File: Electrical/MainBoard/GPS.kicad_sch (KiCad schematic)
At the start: 2 parts, among them U7 MAX-M8C-0

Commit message: Begin layout of pcb
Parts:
- added E1: APAE1590R2540AKDB1-T, RobotLibrary:XDCR_APAE1590R2540AKDB1-T, symbol RobotLibary:APAE1590R2540AKDB1-T
- renumbered U7 to U14
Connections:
- net at U14.11 (RF_IN): now also E1.1
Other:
- note removed: "Antenna DigiKey PN: 2057-ANT-20087EB56-ND Maybe?..."
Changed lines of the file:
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@@
+    (stroke (width 0) (type default))
+  )
+  (wire (pts (xy 79.375 93.345) (xy 105.41 93.345))
     (stroke (width 0) (type default))
   )
@@
     (stroke (width 0) (type default))
   )
+  (wire (pts (xy 79.375 91.44) (xy 79.375 93.345))
+    (stroke (width 0) (type default))
+  )
   (wire (pts (xy 158.75 186.055) (xy 161.925 186.055))
     (stroke (width 0) (type default))
@@
   (wire (pts (xy 99.06 90.805) (xy 105.41 90.805))
     (stroke (width 0) (type default))
-  )
-  (text "Antenna DigiKey PN: 2057-ANT-20087EB56-ND\nMaybe?..."
-    (at 38.1 95.885 0)
-    (effects (font (size 1.27 1.27)) (justify left bottom))
   )
   (hierarchical_label "U2RX" (shape output) (at 155.575 103.505 0) (fields_autoplaced)
@@
         )
         (path "/bd24c4db-4e36-4117-bd4f-5228ef241da9/3efd4746-229a-4377-9033-64e7155c364f"
-          (reference "#PWR083") (unit 1)
+          (reference "#PWR0150") (unit 1)
         )
       )
@@
   (symbol (lib_id "RobotLibary:MAX-M8C-0") (at 128.27 95.885 0) (unit 1)
     (in_bom yes) (on_board yes) (dnp no)
-    (property "Reference" "U7" (at 128.27 74.295 0)
+    (property "Reference" "U14" (at 128.27 74.295 0)
       (effects (font (size 2 2)))
     )
@@
       (project "MainBoard"
         (path "/bd24c4db-4e36-4117-bd4f-5228ef241da9/3efd4746-229a-4377-9033-64e7155c364f"
-          (reference "U7") (unit 1)
+          (reference "U14") (unit 1)
         )
       )
@@
         )
         (path "/bd24c4db-4e36-4117-bd4f-5228ef241da9/3efd4746-229a-4377-9033-64e7155c364f"
-          (reference "C17") (unit 1)
+          (reference "C34") (unit 1)
         )
       )
@@
         )
         (path "/bd24c4db-4e36-4117-bd4f-5228ef241da9/3efd4746-229a-4377-9033-64e7155c364f"
-          (reference "#PWR082") (unit 1)
+          (reference "#PWR0146") (unit 1)
+        )
+      )
+    )
+  )
+  (symbol (lib_id "RobotLibary:APAE1590R2540AKDB1-T") (at 79.375 86.36 0) (unit 1)
+    (in_bom yes) (on_board yes) (dnp no) (fields_autoplaced)
+    (property "Reference" "E1" (at 83.185 83.6295 0)
+      (effects (font (size 1.27 1.27)) (justify left))
+    )
+    (property "Value" "APAE1590R2540AKDB1-T" (at 83.185 86.1695 0)
+      (effects (font (size 1.27 1.27)) (justify left))
+    )
+    (property "Footprint" "RobotLibrary:XDCR_APAE1590R2540AKDB1-T" (at 79.375 86.36 0)
+      (effects (font (size 1.27 1.27)) (justify bottom) hide)
+    )
+    (property "Datasheet" "https://abracon.com/patchantenna/APAE1590R2540AKDB1-T.pdf" (at 79.375 86.36 0)
+      (effects (font (size 1.27 1.27)) hide)
+    )
+    (property "Description" "RF ANT 1.575/1.602GHZ CER PATCH" (at 79.375 86.36 0)
+      (effects (font (size 1.27 1.27)) hide)
+    )
+    (property "Mfr" "Abracon LLC" (at 79.375 86.36 0)
+      (effects (font (size 1.27 1.27)) hide)
+    )
+    (property "Mfr P/N" "APAE1590R2540AKDB1-T" (at 79.375 86.36 0)
+      (effects (font (size 1.27 1.27)) hide)
+    )
+    (property "Supplier 1" "DigiKey" (at 79.375 86.36 0)
+      (effects (font (size 1.27 1.27)) hide)
+    )
+    (property "Supplier 1 P/N" "535-11940-ND" (at 79.375 86.36 0)
+      (effects (font (size 1.27 1.27)) hide)
+    )
+    (property "Supplier 2" "" (at 79.375 86.36 0)
+      (effects (font (size 1.27 1.27)) hide)
+    )
+    (property "Supplier 2 P/N" "" (at 79.375 86.36 0)
+      (effects (font (size 1.27 1.27)) hide)
+    )
+    (pin "1")
+    (instances
+      (project "MainBoard"
+        (path "/bd24c4db-4e36-4117-bd4f-5228ef241da9/3efd4746-229a-4377-9033-64e7155c364f"
+          (reference "E1") (unit 1)
         )
       )
@@
         )
         (path "/bd24c4db-4e36-4117-bd4f-5228ef241da9/3efd4746-229a-4377-9033-64e7155c364f"
-          (reference "#PWR080") (unit 1)
+          (reference "#PWR0148") (unit 1)
         )
       )
@@
         )
         (path "/bd24c4db-4e36-4117-bd4f-5228ef241da9/3efd4746-229a-4377-9033-64e7155c364f"
-          (reference "#PWR079") (unit 1)
+          (reference "#PWR0147") (unit 1)
         )
       )
@@
         )
         (path "/bd24c4db-4e36-4117-bd4f-5228ef241da9/3efd4746-229a-4377-9033-64e7155c364f"
-          (reference "#PWR081") (unit 1)
-        )
-      )
+          (reference "#PWR0149") (unit 1)
+        )
+      )

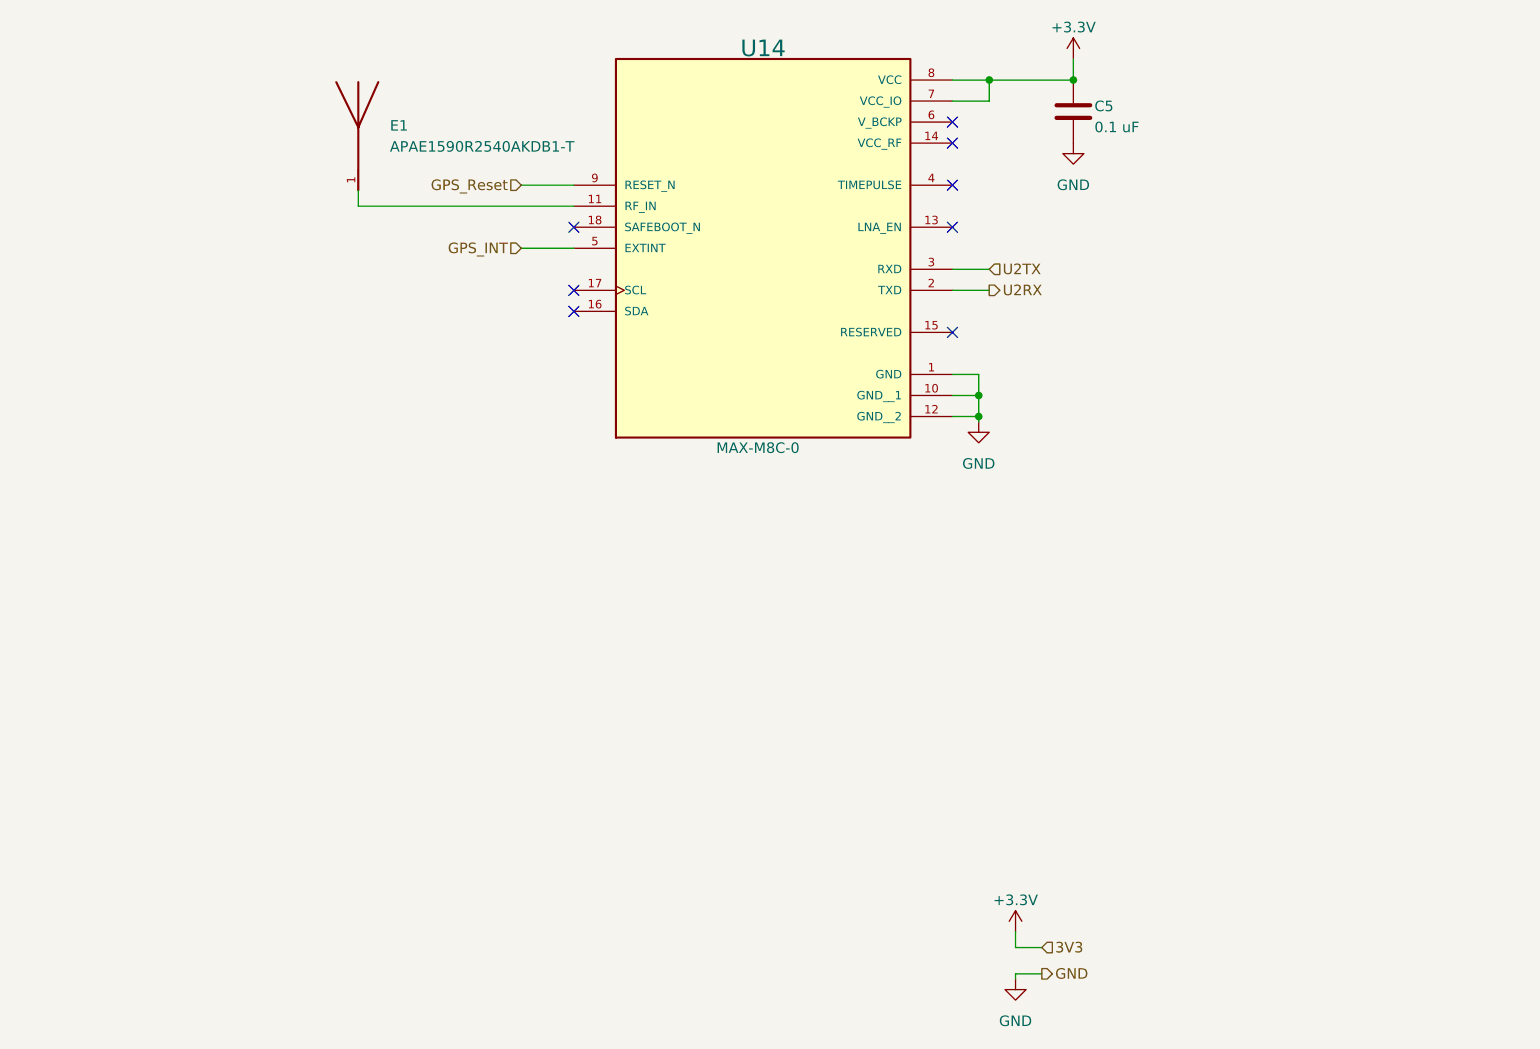
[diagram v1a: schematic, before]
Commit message: First Pass at the routing
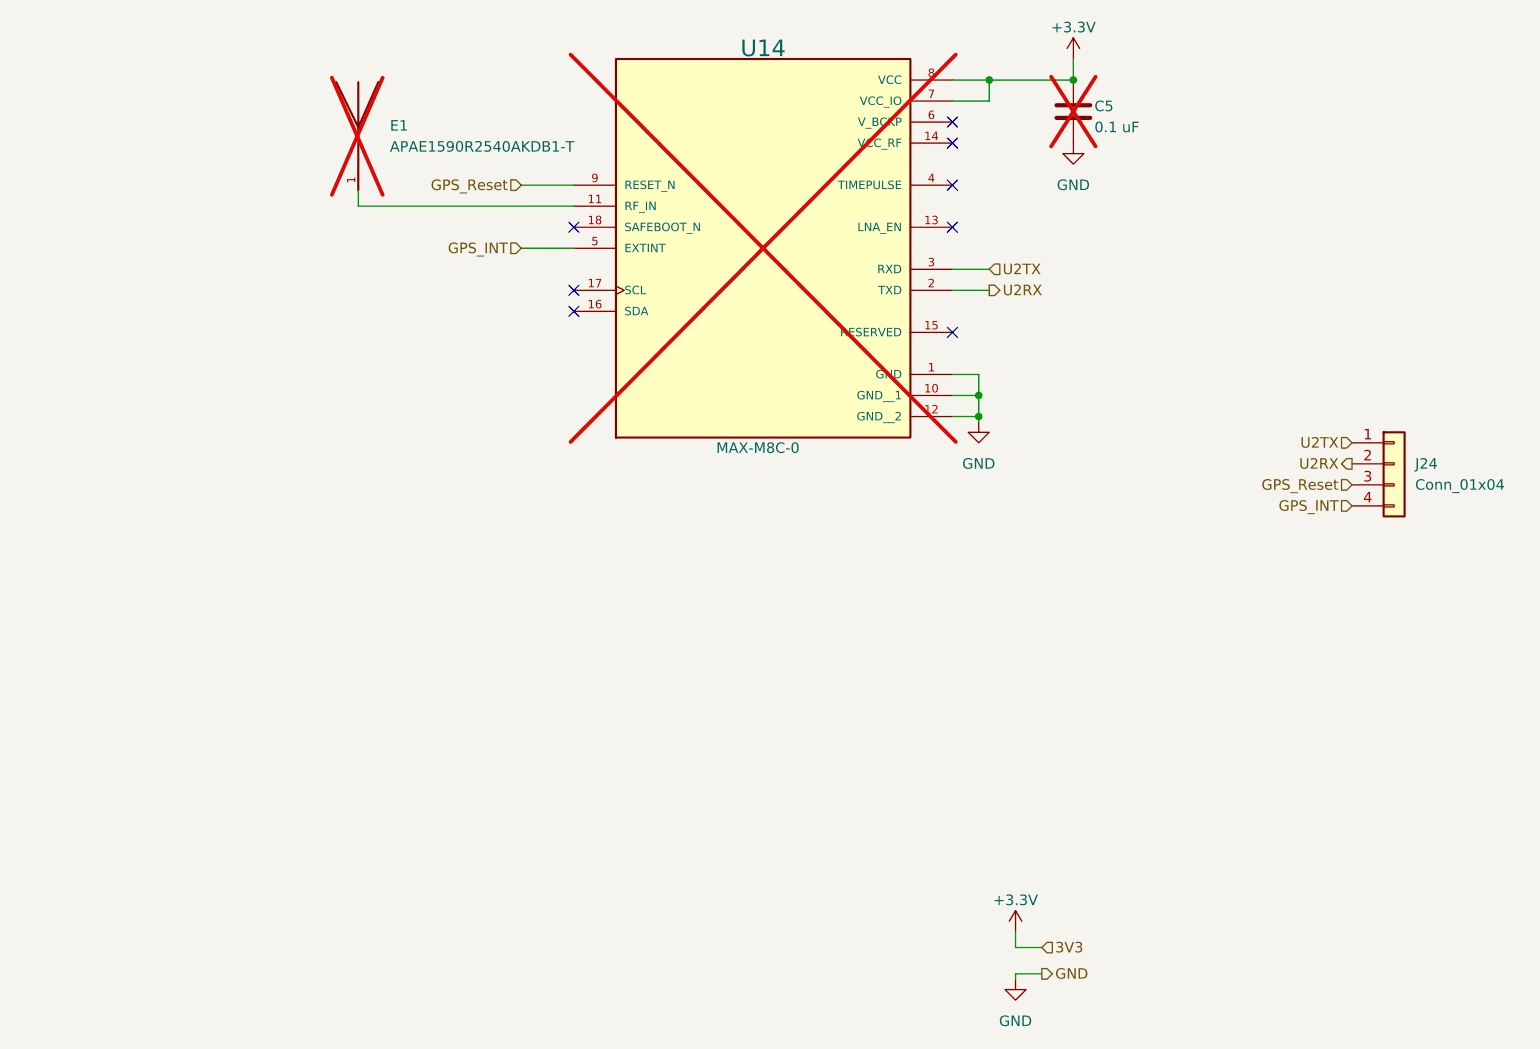
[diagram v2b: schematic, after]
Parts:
- added J24: Conn_01x04, RobotLibrary:CONN_22-23-2041_MOL, symbol Connector_Generic:Conn_01x04
- C5, U14: now not fitted; now left out of the parts list
- E1: MANUFACTURER (none) -> Abracon; MAXIMUM_PACKAGE_HEIGHT (none) -> 4.7mm; PARTREV (none) -> -; SNAPEDA_PN (none) -> APAE1590R2540AKDB1-T; STANDARD (none) -> IPC-7351B; now not fitted; now left out of the parts list
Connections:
- net GPS_INT: now also J24.4 (Pin_4)
- net GPS_Reset: now also J24.3 (Pin_3)
- net U2RX: now also J24.2 (Pin_2)
- net U2TX: now also J24.1 (Pin_1)
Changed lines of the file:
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@@
     (stroke (width 0) (type default))
   )
+  (hierarchical_label "GPS_Reset" (shape input) (at 199.39 127 180) (fields_autoplaced)
+    (effects (font (size 1.27 1.27)) (justify right))
+  )
   (hierarchical_label "U2RX" (shape output) (at 155.575 103.505 0) (fields_autoplaced)
     (effects (font (size 1.27 1.27)) (justify left))
@@
     (effects (font (size 1.27 1.27)) (justify left))
   )
+  (hierarchical_label "U2RX" (shape output) (at 199.39 124.46 180) (fields_autoplaced)
+    (effects (font (size 1.27 1.27)) (justify right))
+  )
   (hierarchical_label "GPS_INT" (shape input) (at 99.06 98.425 180) (fields_autoplaced)
     (effects (font (size 1.27 1.27)) (justify right))
   )
+  (hierarchical_label "U2TX" (shape input) (at 199.39 121.92 180) (fields_autoplaced)
+    (effects (font (size 1.27 1.27)) (justify right))
+  )
+  (hierarchical_label "U2TX" (shape input) (at 155.575 100.965 0) (fields_autoplaced)
+    (effects (font (size 1.27 1.27)) (justify left))
+  )
   (hierarchical_label "GPS_Reset" (shape input) (at 99.06 90.805 180) (fields_autoplaced)
     (effects (font (size 1.27 1.27)) (justify right))
   )
-  (hierarchical_label "U2TX" (shape input) (at 155.575 100.965 0) (fields_autoplaced)
-    (effects (font (size 1.27 1.27)) (justify left))
+  (hierarchical_label "GPS_INT" (shape input) (at 199.39 129.54 180) (fields_autoplaced)
+    (effects (font (size 1.27 1.27)) (justify right))
   )
   (symbol (lib_id "power:GND") (at 165.735 85.725 0) (unit 1)
@@
     )
   )
+  (symbol (lib_id "Connector_Generic:Conn_01x04") (at 204.47 124.46 0) (unit 1)
+    (in_bom yes) (on_board yes) (dnp no) (fields_autoplaced)
+    (property "Reference" "J24" (at 207.01 124.46 0)
+      (effects (font (size 1.27 1.27)) (justify left))
+    )
+    (property "Value" "Conn_01x04" (at 207.01 127 0)
+      (effects (font (size 1.27 1.27)) (justify left))
+    )
+    (property "Footprint" "RobotLibrary:CONN_22-23-2041_MOL" (at 204.47 124.46 0)
+      (effects (font (size 1.27 1.27)) hide)
+    )
+    (property "Datasheet" "~" (at 204.47 124.46 0)
+      (effects (font (size 1.27 1.27)) hide)
+    )
+    (property "Description" "" (at 204.47 124.46 0)
+      (effects (font (size 1.27 1.27)) hide)
+    )
+    (property "Mfr" "" (at 204.47 124.46 0)
+      (effects (font (size 1.27 1.27)) hide)
+    )
+    (property "Mfr P/N" "" (at 204.47 124.46 0)
+      (effects (font (size 1.27 1.27)) hide)
+    )
+    (property "Supplier 1" "" (at 204.47 124.46 0)
+      (effects (font (size 1.27 1.27)) hide)
+    )
+    (property "Supplier 1 P/N" "" (at 204.47 124.46 0)
+      (effects (font (size 1.27 1.27)) hide)
+    )
+    (property "Supplier 2" "" (at 204.47 124.46 0)
+      (effects (font (size 1.27 1.27)) hide)
+    )
+    (property "Supplier 2 P/N" "" (at 204.47 124.46 0)
+      (effects (font (size 1.27 1.27)) hide)
+    )
+    (pin "1")
+    (pin "2")
+    (pin "3")
+    (pin "4")
+    (instances
+      (project "MainBoard"
+        (path "/bd24c4db-4e36-4117-bd4f-5228ef241da9/3efd4746-229a-4377-9033-64e7155c364f"
+          (reference "J24") (unit 1)
+        )
+      )
+    )
+  )
   (symbol (lib_id "RobotLibary:MAX-M8C-0") (at 128.27 95.885 0) (unit 1)
-    (in_bom yes) (on_board yes) (dnp no)
+    (in_bom no) (on_board no) (dnp yes)
     (property "Reference" "U14" (at 128.27 74.295 0)
       (effects (font (size 2 2)))
@@
     )
     (property "Datasheet" "https://www.u-blox.com/en/docs/UBX-16000093" (at 128.27 95.885 0)
+      (effects (font (size 1.27 1.27)) hide)
+    )
+    (property "Description" "" (at 128.27 95.885 0)
+      (effects (font (size 1.27 1.27)) hide)
+    )
+    (property "Mfr" "" (at 128.27 95.885 0)
+      (effects (font (size 1.27 1.27)) hide)
+    )
+    (property "Mfr P/N" "" (at 128.27 95.885 0)
+      (effects (font (size 1.27 1.27)) hide)
+    )
+    (property "Supplier 1" "" (at 128.27 95.885 0)
+      (effects (font (size 1.27 1.27)) hide)
+    )
+    (property "Supplier 1 P/N" "" (at 128.27 95.885 0)
+      (effects (font (size 1.27 1.27)) hide)
+    )
+    (property "Supplier 2" "" (at 128.27 95.885 0)
+      (effects (font (size 1.27 1.27)) hide)
+    )
+    (property "Supplier 2 P/N" "" (at 128.27 95.885 0)
       (effects (font (size 1.27 1.27)) hide)
     )
@@
   )
   (symbol (lib_id "Device:C") (at 165.735 81.915 0) (unit 1)
-    (in_bom yes) (on_board yes) (dnp no)
+    (in_bom no) (on_board no) (dnp yes)
     (property "Reference" "C5" (at 168.275 81.28 0)
       (effects (font (size 1.27 1.27)) (justify left))
@@
   )
   (symbol (lib_id "RobotLibary:APAE1590R2540AKDB1-T") (at 79.375 86.36 0) (unit 1)
-    (in_bom yes) (on_board yes) (dnp no) (fields_autoplaced)
+    (in_bom no) (on_board no) (dnp yes) (fields_autoplaced)
     (property "Reference" "E1" (at 83.185 83.6295 0)
       (effects (font (size 1.27 1.27)) (justify left))
@@
       (effects (font (size 1.27 1.27)) hide)
     )
-    (pin "1")
+    (property "PARTREV" "-" (at 79.375 86.36 0)
+      (effects (font (size 1.27 1.27)) (justify bottom) hide)
+    )
+    (property "SNAPEDA_PN" "APAE1590R2540AKDB1-T" (at 79.375 86.36 0)
+      (effects (font (size 1.27 1.27)) (justify bottom) hide)
+    )
+    (property "STANDARD" "IPC-7351B" (at 79.375 86.36 0)
+      (effects (font (size 1.27 1.27)) (justify bottom) hide)
+    )
+    (property "MAXIMUM_PACKAGE_HEIGHT" "4.7mm" (at 79.375 86.36 0)
+      (effects (font (size 1.27 1.27)) (justify bottom) hide)
+    )
+    (property "MANUFACTURER" "Abracon" (at 79.375 86.36 0)
+      (effects (font (size 1.27 1.27)) (justify bottom) hide)
+    )
+    (pin "1")

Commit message: Add some finishing touches and create preliminary boms
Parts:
- J24: Mfr (none) -> Molex; Mfr P/N (none) -> 0022232041; Supplier 1 (none) -> DigiKey; Supplier 1 P/N (none) -> WM4202-ND
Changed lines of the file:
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@@
       (effects (font (size 1.27 1.27)) hide)
     )
-    (property "Mfr" "" (at 204.47 124.46 0)
+    (property "Mfr" "Molex" (at 204.47 124.46 0)
       (effects (font (size 1.27 1.27)) hide)
     )
-    (property "Mfr P/N" "" (at 204.47 124.46 0)
+    (property "Mfr P/N" "0022232041" (at 204.47 124.46 0)
       (effects (font (size 1.27 1.27)) hide)
     )
-    (property "Supplier 1" "" (at 204.47 124.46 0)
+    (property "Supplier 1" "DigiKey" (at 204.47 124.46 0)
       (effects (font (size 1.27 1.27)) hide)
     )
-    (property "Supplier 1 P/N" "" (at 204.47 124.46 0)
+    (property "Supplier 1 P/N" "WM4202-ND" (at 204.47 124.46 0)
       (effects (font (size 1.27 1.27)) hide)
     )

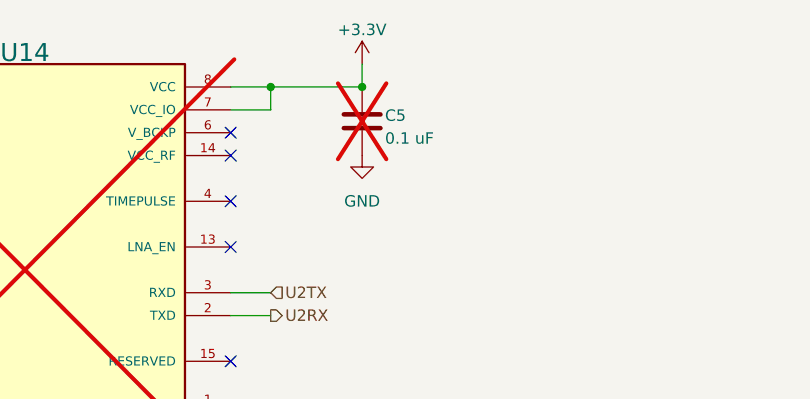
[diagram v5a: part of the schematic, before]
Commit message: Fix SPI3 and make visual improvements
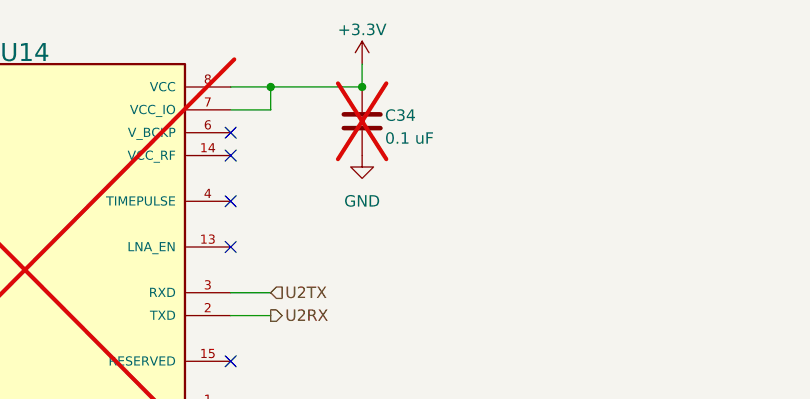
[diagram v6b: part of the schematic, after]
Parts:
- renumbered C5 to C34
